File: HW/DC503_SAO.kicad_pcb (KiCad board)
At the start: 2 copper layers, 54.9 x 39.2 mm, 21 parts, among them J1 GS2, J2 GS2, U1 ATTINY85-20SU, X1 Badgelife_shitty_connector

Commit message: moved the Diode symbole down on footprint, updated PCB layout.
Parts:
- moved D1 1.24 mm to (154.6, 73.8), turned to 270 degrees

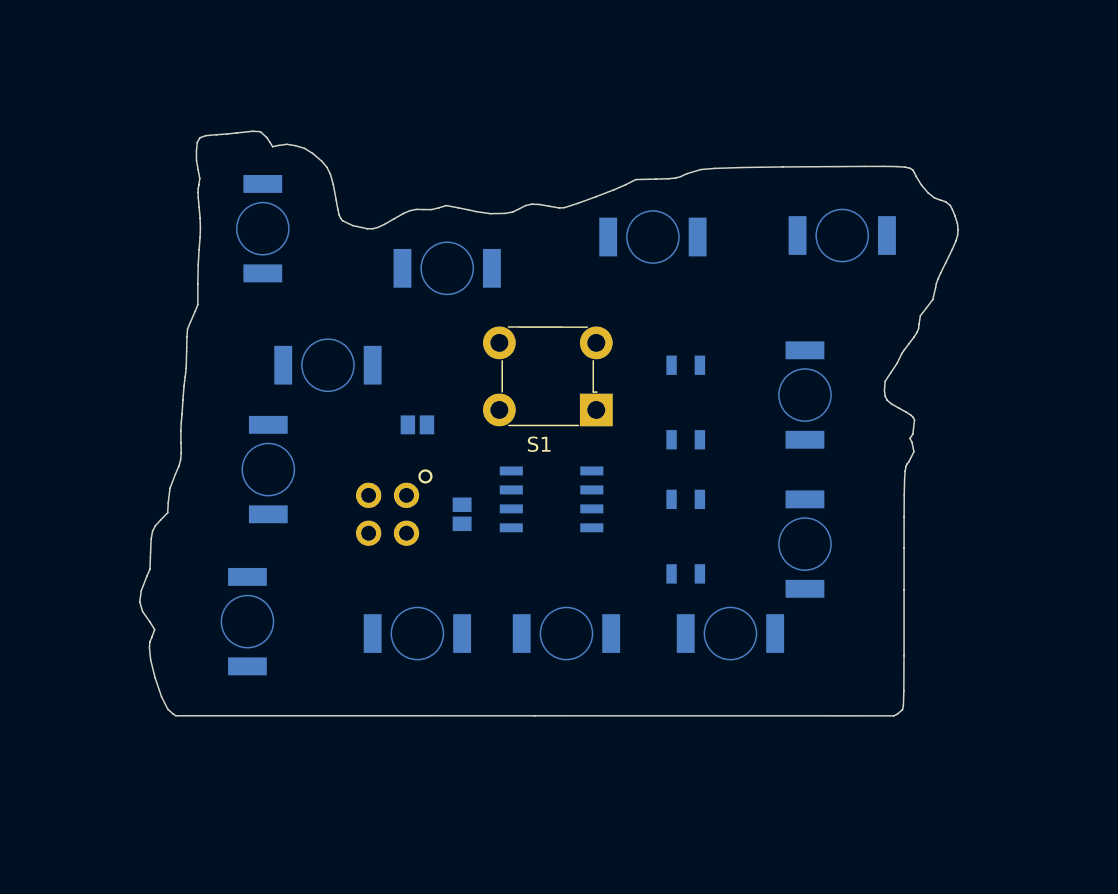
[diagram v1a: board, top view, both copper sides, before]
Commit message: cleaning up art files, changed process to do svg to bmp to kicad
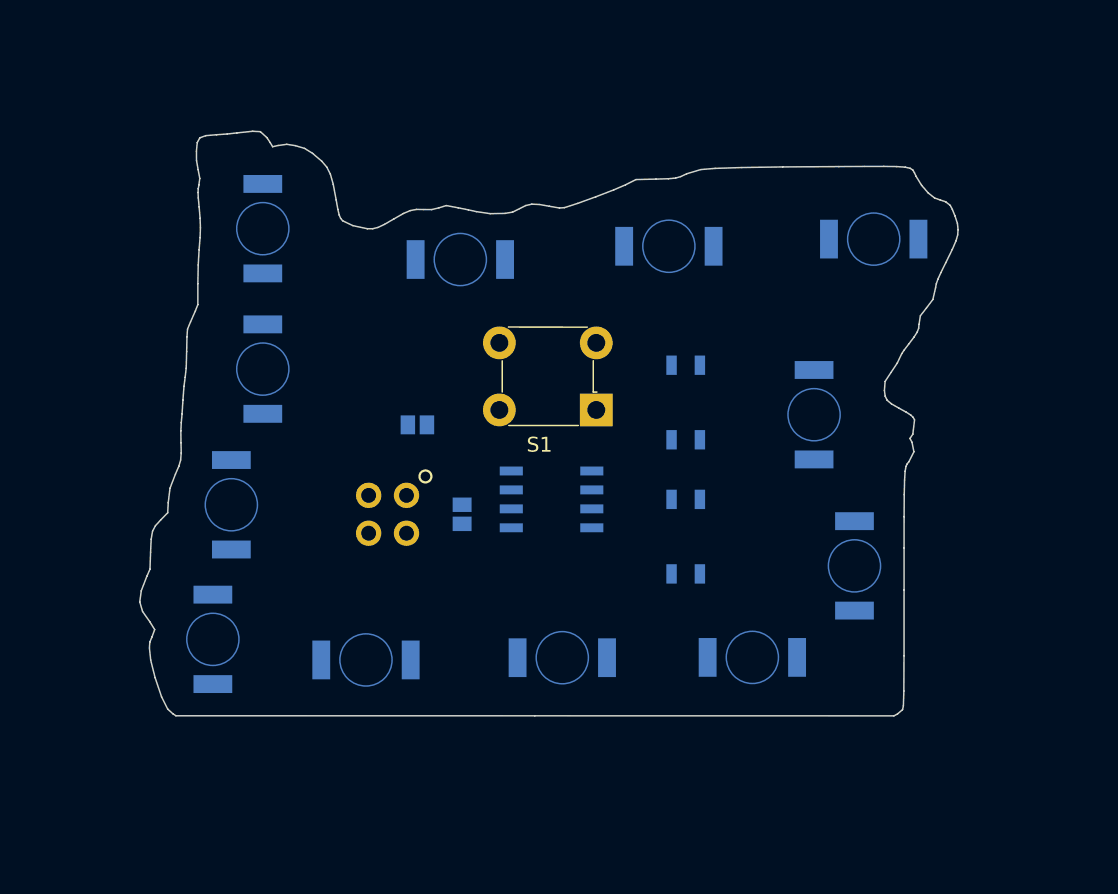
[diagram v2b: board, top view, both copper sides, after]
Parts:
- moved D12 4.38 mm to (154.6, 83.3), turned to 90 degrees
- moved D9 3.88 mm to (161.6, 102.8)
- moved D6 3.63 mm to (194.3, 96.5)
- moved D11 3.42 mm to (152.5, 92.4)
- moved D10 2.61 mm to (151.3, 101.4)
- moved D7 2.17 mm to (187.5, 102.6)
- moved D4 2.12 mm to (195.6, 74.5)
- moved D8 1.64 mm to (174.7, 102.6)
- moved D5 1.45 mm to (191.6, 86.3)
- moved D3 1.24 mm to (181.9, 75.0), turned to 180 degrees
- moved D2 1.06 mm to (167.9, 75.9)
- turned U1 to 180 degrees
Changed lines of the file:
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@@
   )
   (module Housings_SOIC:SOIC-8_3.9x4.9mm_Pitch1.27mm (layer B.Cu)
-    (at 174 92)
+    (at 174 92 180)
     (descr "8-Lead Plastic Small Outline (SN) - Narrow, 3.90 mm Body [SOIC] (see Microchip Packaging Specification 00000049BS.pdf)")
     (tags "SOIC 1.27")
     (attr smd)
-    (fp_text reference U1 (at 0 3.5) (layer B.SilkS)
-      (effects (font (size 1 1) (thickness 0.15)) (justify mirror))
-    )
-    (fp_text value ATTINY85-20SU (at 0 -3.5) (layer B.Fab)
-      (effects (font (size 1 1) (thickness 0.15)) (justify mirror))
-    )
-    (fp_text user %R (at 0 0) (layer B.Fab)
+    (fp_text reference U1 (at 0 3.5 180) (layer B.SilkS)
+      (effects (font (size 1 1) (thickness 0.15)) (justify mirror))
+    )
+    (fp_text value ATTINY85-20SU (at 0 -3.5 180) (layer B.Fab)
+      (effects (font (size 1 1) (thickness 0.15)) (justify mirror))
+    )
+    (fp_text user %R (at 0 0 180) (layer B.Fab)
       (effects (font (size 1 1) (thickness 0.15)) (justify mirror))
     )
@@
     (fp_line (start -2.075 -2.575) (end 2.075 -2.575) (layer B.SilkS) (width 0.15))
     (fp_line (start -2.075 2.525) (end -3.475 2.525) (layer B.SilkS) (width 0.15))
-    (pad 1 smd rect (at -2.7 1.905) (size 1.55 0.6) (layers B.Cu B.Paste B.Mask)
+    (pad 1 smd rect (at -2.7 1.905 180) (size 1.55 0.6) (layers B.Cu B.Paste B.Mask)
       (net 13 "Net-(U1-Pad1)"))
-    (pad 2 smd rect (at -2.7 0.635) (size 1.55 0.6) (layers B.Cu B.Paste B.Mask)
-      (net 4 /ROW4))
-    (pad 3 smd rect (at -2.7 -0.635) (size 1.55 0.6) (layers B.Cu B.Paste B.Mask)
+    (pad 2 smd rect (at -2.7 0.635 180) (size 1.55 0.6) (layers B.Cu B.Paste B.Mask)
+      (net 4 /ROW4))
+    (pad 3 smd rect (at -2.7 -0.635 180) (size 1.55 0.6) (layers B.Cu B.Paste B.Mask)
       (net 12 /BUTTON))
-    (pad 4 smd rect (at -2.7 -1.905) (size 1.55 0.6) (layers B.Cu B.Paste B.Mask)
+    (pad 4 smd rect (at -2.7 -1.905 180) (size 1.55 0.6) (layers B.Cu B.Paste B.Mask)
       (net 11 GND))
-    (pad 5 smd rect (at 2.7 -1.905) (size 1.55 0.6) (layers B.Cu B.Paste B.Mask)
+    (pad 5 smd rect (at 2.7 -1.905 180) (size 1.55 0.6) (layers B.Cu B.Paste B.Mask)
       (net 6 /ROW1))
-    (pad 6 smd rect (at 2.7 -0.635) (size 1.55 0.6) (layers B.Cu B.Paste B.Mask)
+    (pad 6 smd rect (at 2.7 -0.635 180) (size 1.55 0.6) (layers B.Cu B.Paste B.Mask)
       (net 2 /ROW2))
-    (pad 7 smd rect (at 2.7 0.635) (size 1.55 0.6) (layers B.Cu B.Paste B.Mask)
+    (pad 7 smd rect (at 2.7 0.635 180) (size 1.55 0.6) (layers B.Cu B.Paste B.Mask)
       (net 3 /ROW3))
-    (pad 8 smd rect (at 2.7 1.905) (size 1.55 0.6) (layers B.Cu B.Paste B.Mask)
+    (pad 8 smd rect (at 2.7 1.905 180) (size 1.55 0.6) (layers B.Cu B.Paste B.Mask)
       (net 14 +3V3))
     (model ${KISYS3DMOD}/Housings_SOIC.3dshapes/SOIC-8_3.9x4.9mm_Pitch1.27mm.wrl
@@
   )
   (module DC503_SAO:OSRAM_LED (layer F.Cu)
-    (at 167 76.5 180)
+    (at 167.88 75.91 180)
     (fp_text reference D2 (at 0 -3.2 180) (layer B.SilkS)
       (effects (font (size 1 1) (thickness 0.15)) (justify mirror))
@@
   )
   (module DC503_SAO:OSRAM_LED (layer F.Cu)
-    (at 153.6 100.2 90)
+    (at 151.28 101.39 90)
     (fp_text reference D10 (at 0 -3.2 90) (layer B.SilkS)
       (effects (font (size 1 1) (thickness 0.15)) (justify mirror))
@@
   )
   (module DC503_SAO:OSRAM_LED (layer F.Cu)
-    (at 193.5 74.3)
+    (at 195.61 74.54)
     (fp_text reference D4 (at 0 -3.2) (layer B.SilkS)
       (effects (font (size 1 1) (thickness 0.15)) (justify mirror))
@@
   )
   (module DC503_SAO:OSRAM_LED (layer F.Cu)
-    (at 180.8 74.4)
-    (fp_text reference D3 (at 0 -3.2) (layer B.SilkS)
-      (effects (font (size 1 1) (thickness 0.15)) (justify mirror))
-    )
-    (fp_text value LED (at 0 -2) (layer B.Fab)
-      (effects (font (size 1 1) (thickness 0.15)) (justify mirror))
-    )
-    (fp_poly (pts (xy -1 1.75) (xy 1 1.75) (xy 1.75 0.75) (xy 1.75 -0.75)
-      (xy 1 -1.75) (xy -1 -1.75) (xy -1.75 -0.75) (xy -1.75 0.75)
-      (xy -1.75 0.75)) (layer B.Mask) (width 0.15))
-    (fp_circle (center 0 0) (end 1.75 0) (layer B.Cu) (width 0.1))
-    (fp_line (start -0.45 3.55) (end -0.45 2.25) (layer B.SilkS) (width 0.25))
-    (fp_line (start 0.45 3.55) (end 0.45 2.35) (layer B.SilkS) (width 0.25))
-    (fp_line (start 0.45 2.35) (end -0.35 2.95) (layer B.SilkS) (width 0.25))
-    (fp_line (start -0.35 2.95) (end 0.45 3.55) (layer B.SilkS) (width 0.25))
-    (pad 1 smd rect (at 3 0) (size 1.2 2.6) (layers B.Cu B.Paste B.SilkS B.Mask)
-      (net 4 /ROW4))
-    (pad 2 smd rect (at -3 0) (size 1.2 2.6) (layers B.Cu B.Paste B.SilkS B.Mask)
-      (net 1 "Net-(D1-Pad2)"))
-  )
-  (module DC503_SAO:OSRAM_LED (layer F.Cu)
-    (at 191 85 90)
+    (at 191.61 86.32 90)
     (fp_text reference D5 (at 0 -3.2 90) (layer B.SilkS)
       (effects (font (size 1 1) (thickness 0.15)) (justify mirror))
@@
   )
   (module DC503_SAO:OSRAM_LED (layer F.Cu)
-    (at 191 95 90)
+    (at 194.32 96.46 90)
     (fp_text reference D6 (at 0 -3.2 90) (layer B.SilkS)
       (effects (font (size 1 1) (thickness 0.15)) (justify mirror))
@@
   )
   (module DC503_SAO:OSRAM_LED (layer F.Cu)
-    (at 186 101)
+    (at 187.47 102.6)
     (fp_text reference D7 (at 0 -3.2) (layer B.SilkS)
       (effects (font (size 1 1) (thickness 0.15)) (justify mirror))
@@
   )
   (module DC503_SAO:OSRAM_LED (layer F.Cu)
-    (at 175 101)
+    (at 174.72 102.62)
     (fp_text reference D8 (at 0 -3.2) (layer B.SilkS)
       (effects (font (size 1 1) (thickness 0.15)) (justify mirror))
@@
   )
   (module DC503_SAO:OSRAM_LED (layer F.Cu)
-    (at 165 101)
+    (at 161.55 102.77)
     (fp_text reference D9 (at 0 -3.2) (layer B.SilkS)
       (effects (font (size 1 1) (thickness 0.15)) (justify mirror))
@@
   )
   (module DC503_SAO:OSRAM_LED (layer F.Cu)
-    (at 155 90 90)
+    (at 152.52 92.36 90)
     (fp_text reference D11 (at 0 -3.2 90) (layer B.SilkS)
       (effects (font (size 1 1) (thickness 0.15)) (justify mirror))
@@
   )
   (module DC503_SAO:OSRAM_LED (layer F.Cu)
-    (at 159 83 180)
-    (fp_text reference D12 (at 0 -3.2 180) (layer B.SilkS)
+    (at 154.63 83.26 90)
+    (fp_text reference D12 (at 0 -3.2 90) (layer B.SilkS)
+      (effects (font (size 1 1) (thickness 0.15)) (justify mirror))
+    )
+    (fp_text value LED (at 0 -2 90) (layer B.Fab)
+      (effects (font (size 1 1) (thickness 0.15)) (justify mirror))
+    )
+    (fp_poly (pts (xy -1 1.75) (xy 1 1.75) (xy 1.75 0.75) (xy 1.75 -0.75)
+      (xy 1 -1.75) (xy -1 -1.75) (xy -1.75 -0.75) (xy -1.75 0.75)
+      (xy -1.75 0.75)) (layer B.Mask) (width 0.15))
+    (fp_circle (center 0 0) (end 1.75 0) (layer B.Cu) (width 0.1))
+    (fp_line (start -0.45 3.55) (end -0.45 2.25) (layer B.SilkS) (width 0.25))
+    (fp_line (start 0.45 3.55) (end 0.45 2.35) (layer B.SilkS) (width 0.25))
+    (fp_line (start 0.45 2.35) (end -0.35 2.95) (layer B.SilkS) (width 0.25))
+    (fp_line (start -0.35 2.95) (end 0.45 3.55) (layer B.SilkS) (width 0.25))
+    (pad 1 smd rect (at 3 0 90) (size 1.2 2.6) (layers B.Cu B.Paste B.SilkS B.Mask)
+      (net 4 /ROW4))
+    (pad 2 smd rect (at -3 0 90) (size 1.2 2.6) (layers B.Cu B.Paste B.SilkS B.Mask)
+      (net 8 "Net-(D10-Pad2)"))
+  )
+  (module DC503_SAO:OSRAM_LED (layer F.Cu)
+    (at 181.87 75.02 180)
+    (fp_text reference D3 (at 0 -3.2 180) (layer B.SilkS)
       (effects (font (size 1 1) (thickness 0.15)) (justify mirror))
     )
@@
       (net 4 /ROW4))
     (pad 2 smd rect (at -3 0 180) (size 1.2 2.6) (layers B.Cu B.Paste B.SilkS B.Mask)
-      (net 8 "Net-(D10-Pad2)"))
+      (net 1 "Net-(D1-Pad2)"))
   )
   (gr_line (start 148.798756 106.51531) (end 148.593429 106.38026) (layer Edge.Cuts) (width 0.1))

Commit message: Got the art done. organized art directory
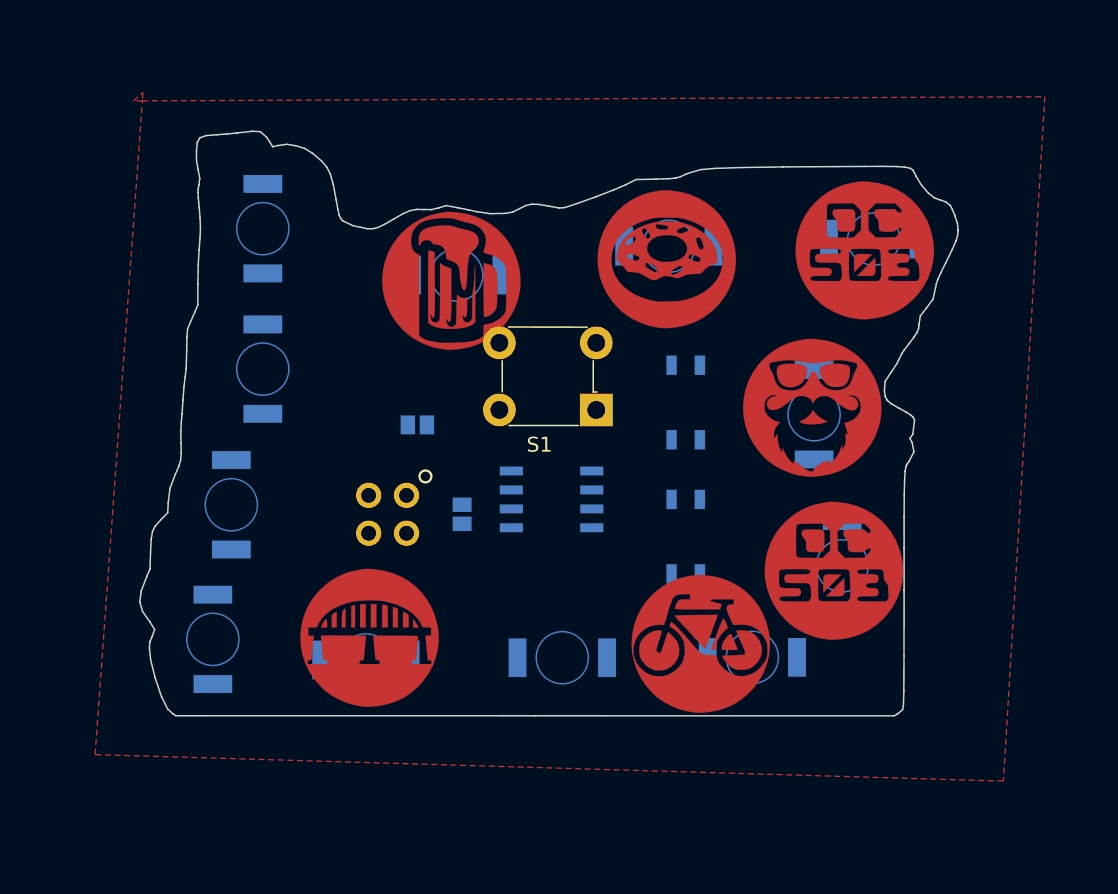
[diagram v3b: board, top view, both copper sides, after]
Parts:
- added G***: LOGO, DC503_SAO:beard_glasses, F.Cu at (191.5, 85.9)
- added G***: LOGO, DC503_SAO:DC_503, F.Cu at (195.0, 75.3)
- added G***: LOGO, DC503_SAO:donut, F.Cu at (181.7, 75.9)
- added G***: LOGO, DC503_SAO:DC_503, F.Cu at (192.9, 96.8)
- added G***: LOGO, DC503_SAO:bike, F.Cu at (184.0, 101.7)
- added G***: LOGO, DC503_SAO:beer, F.Cu at (167.3, 77.4)
- added G***: LOGO, DC503_SAO:bridge, F.Cu at (161.8, 101.3)
- moved D2 1.07 mm to (167.6, 77.0)
- moved D6 0.82 mm to (193.5, 96.5)
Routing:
- added copper zone on F.Cu, net GND

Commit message: finialized art
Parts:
- removed the G*** at (192.9, 96.8)
- added G***: LOGO, DC503_SAO:DC_503, F.Cu at (183.0, 104.2)
- added G***: LOGO, DC503_SAO:DC_503, F.Cu at (149.0, 104.2)
- added G***: LOGO, DC503_SAO:DC_503, F.Cu at (197.0, 93.2)
- added G***: LOGO, DC503_SAO:DC_503, F.Cu at (200.0, 72.5)
- added G***: LOGO, DC503_SAO:rain, F.Cu at (166.5, 104.2)
- added G***: LOGO, DC503_SAO:heart, F.Cu at (174.6, 124.4)
- added G***: LOGO, DC503_SAO:DC_503, F.Cu at (152.0, 81.0)
- X1: footprint DC503_SAO:Badgelife-Shitty-2x2 -> Badgelife-Shitty-2x2
- moved G*** 44.5 mm to (152.5, 70.2)
- moved G*** 38.4 mm to (195.5, 83.0)
- moved G*** 35.9 mm to (150.2, 93.2)
- moved G*** 28.5 mm to (166.5, 75.0)
- moved G*** 19.2 mm to (197.0, 104.2)
- moved G*** 16.3 mm to (183.0, 73.0)
- moved D7 6.49 mm to (193.5, 105.0)
- moved S1 5.89 mm to (176.8, 91.9)
- moved D5 5.89 mm to (197.5, 86.3)
- moved D12 4.56 mm to (151.0, 80.5)
- moved D6 4.52 mm to (198.0, 96.0)
- moved D8 4.05 mm to (178.0, 105.0)
- moved D1 3.72 mm to (153.0, 70.5), turned to 180 degrees
- moved D11 3.54 mm to (149.0, 92.0)
- moved D10 3.11 mm to (149.0, 103.5)
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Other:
- board size 54.9 x 39.2 mm -> 63.1 x 45.1 mm

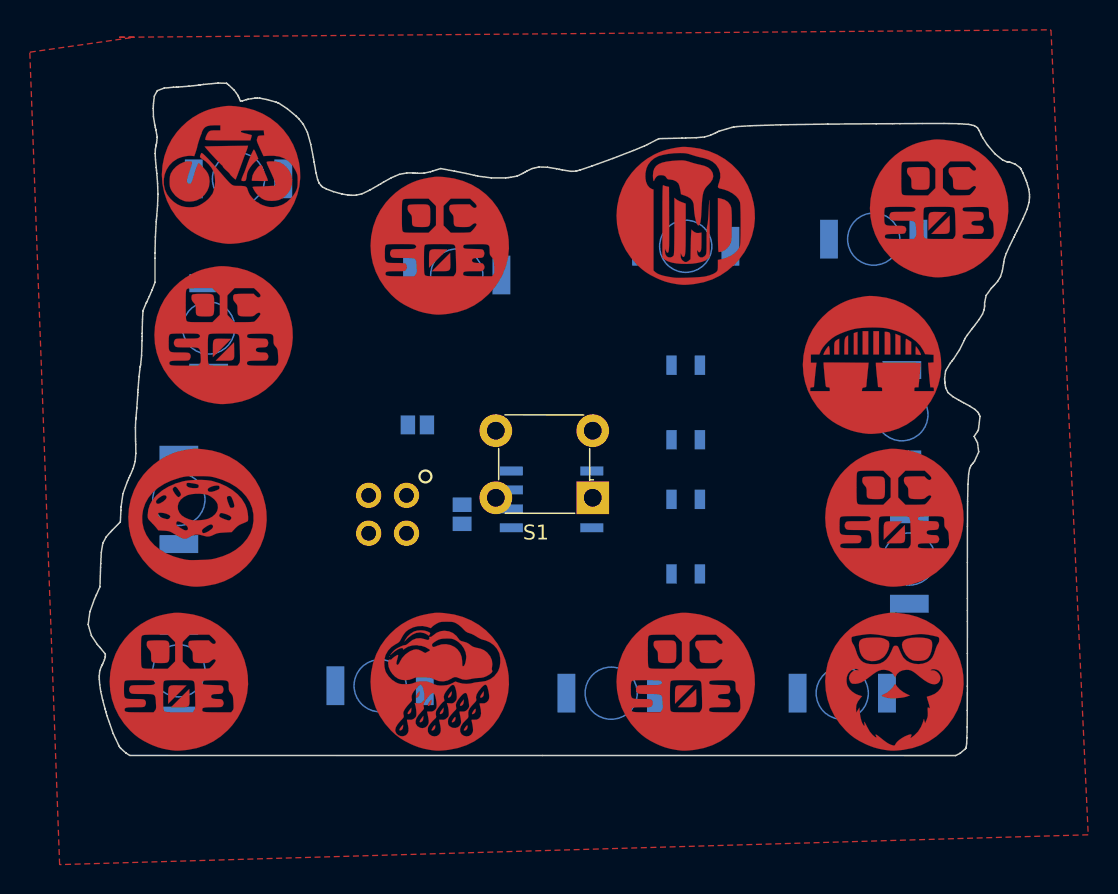
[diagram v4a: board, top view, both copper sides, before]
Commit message: moving LED's arround, top layer art done
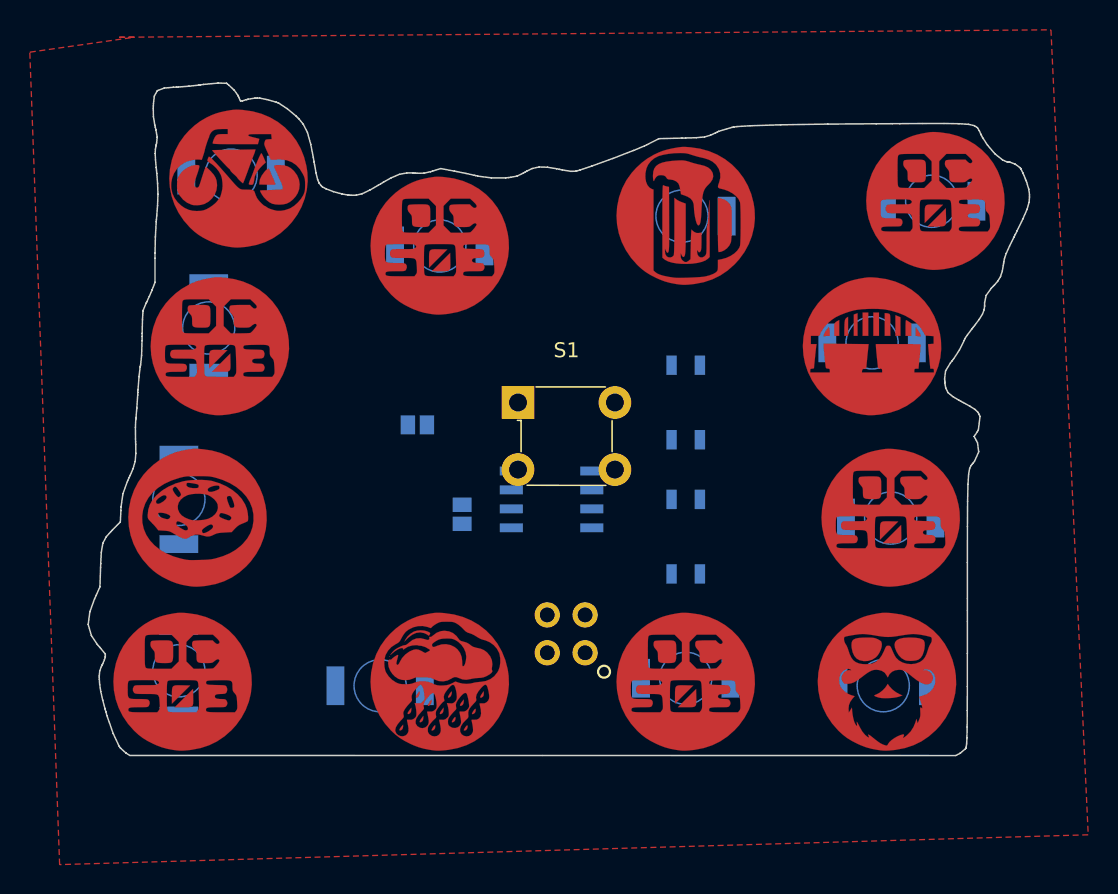
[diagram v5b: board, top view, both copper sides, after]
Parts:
- moved G*** 34.9 mm to (175.0, 89.5)
- moved X1 14.4 mm to (175.0, 101.0), turned to 180 degrees
- moved S1 8.12 mm to (171.8, 85.5), turned to 0 degrees
- moved D5 5.22 mm to (195.5, 81.5), turned to 180 degrees
- moved D8 5.10 mm to (183.0, 104.0)
- moved D4 4.65 mm to (199.5, 72.0), turned to 180 degrees
- moved D6 3.02 mm to (196.8, 93.2), turned to 180 degrees
- moved D7 2.80 mm to (196.2, 104.5), turned to 180 degrees
- moved D2 2.26 mm to (166.5, 75.0)
- moved D3 2.04 mm to (182.8, 73.0), turned to 180 degrees
- moved G*** 1.25 mm to (195.5, 81.8)
- moved G*** 0.79 mm to (151.8, 81.8)
- moved D1 0.56 mm to (152.5, 70.2)
- moved G*** 0.56 mm to (199.8, 72.0)
- moved G*** 0.56 mm to (153.0, 70.5)
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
